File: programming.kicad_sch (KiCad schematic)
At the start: 14 parts, among them U1 LFE5U-12F-6BG256C, U2 AT25SF081-SSHD-X

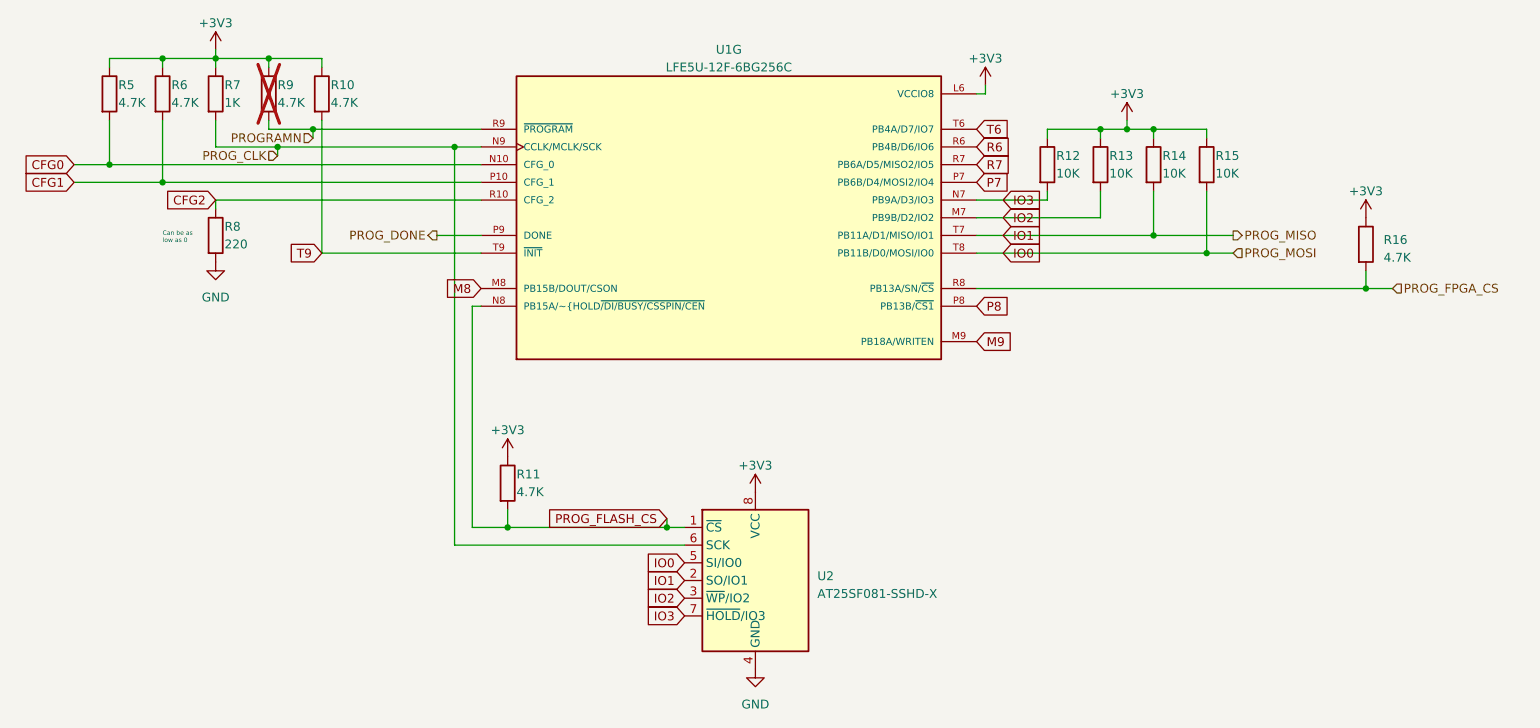
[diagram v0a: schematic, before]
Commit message: Small routing tweaks, add breakout to schematic
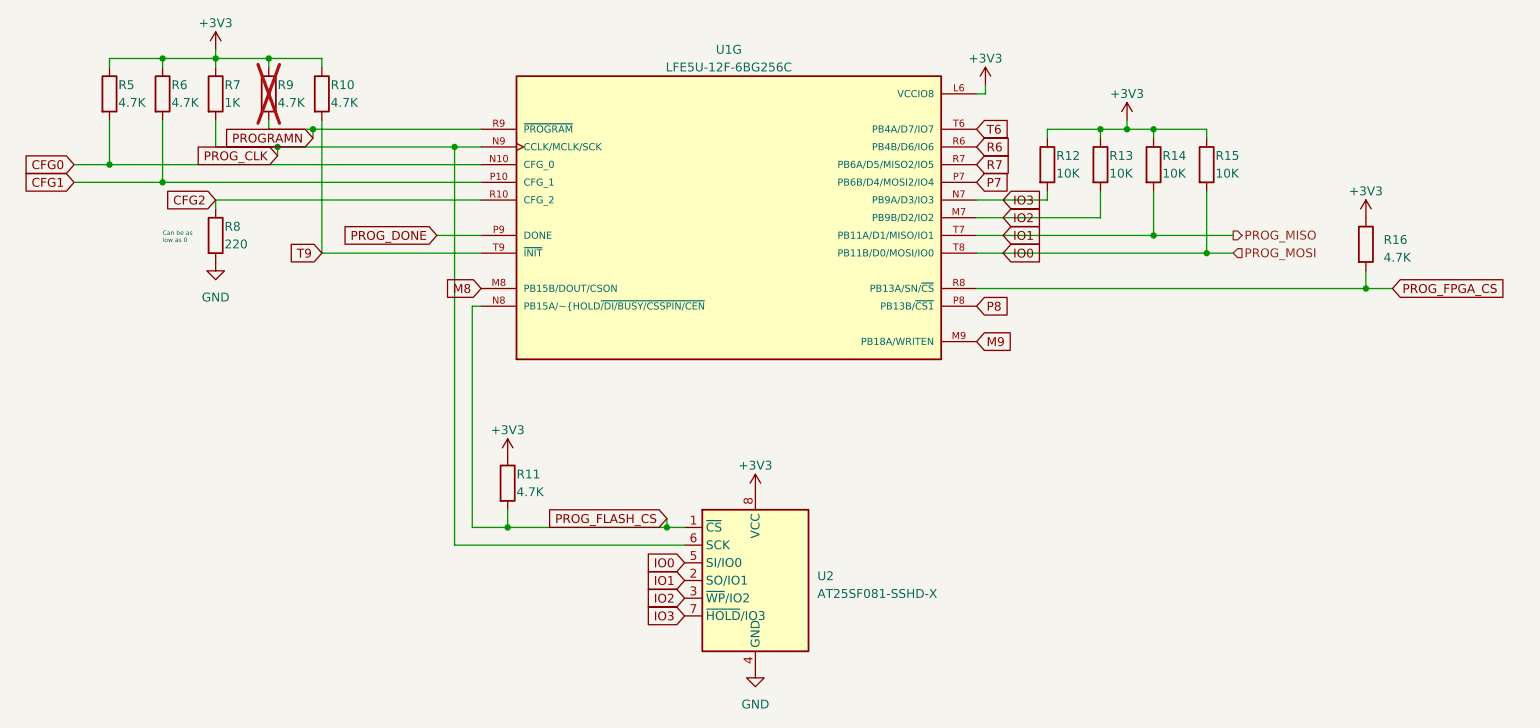
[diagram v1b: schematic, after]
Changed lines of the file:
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@@
     (effects (font (size 0.635 0.635)) (justify left bottom))
+  )
+  (global_label "PROG_FPGA_CS" (shape input) (at 242.57 85.09 0) (fields_autoplaced)
+    (effects (font (size 1.27 1.27)) (justify left))
+    (property "Intersheetrefs" "${INTERSHEET_REFS}" (at 259.7482 85.09 0)
+      (effects (font (size 1.27 1.27)) (justify left) hide)
+    )
   )
   (global_label "IO2" (shape input) (at 140.97 129.54 180) (fields_autoplaced)
@@
     )
   )
+  (global_label "PROG_DONE" (shape input) (at 105.41 77.47 180) (fields_autoplaced)
+    (effects (font (size 1.27 1.27)) (justify right))
+    (property "Intersheetrefs" "${INTERSHEET_REFS}" (at 91.3161 77.47 0)
+      (effects (font (size 1.27 1.27)) (justify right) hide)
+    )
+  )
   (global_label "M8" (shape input) (at 111.76 85.09 180) (fields_autoplaced)
     (effects (font (size 1.27 1.27)) (justify right))
@@
     )
   )
-  (hierarchical_label "PROG_DONE" (shape output) (at 105.41 77.47 180) (fields_autoplaced)
+  (global_label "PROGRAMN" (shape input) (at 87.63 63.5 180) (fields_autoplaced)
     (effects (font (size 1.27 1.27)) (justify right))
+    (property "Intersheetrefs" "${INTERSHEET_REFS}" (at 74.4432 63.5 0)
+      (effects (font (size 1.27 1.27)) (justify right) hide)
+    )
   )
-  (hierarchical_label "PROGRAMN" (shape input) (at 87.63 63.5 180) (fields_autoplaced)
+  (global_label "PROG_CLK" (shape input) (at 82.55 66.04 180) (fields_autoplaced)
     (effects (font (size 1.27 1.27)) (justify right))
+    (property "Intersheetrefs" "${INTERSHEET_REFS}" (at 69.968 66.04 0)
+      (effects (font (size 1.27 1.27)) (justify right) hide)
+    )
+  )
+  (hierarchical_label "PROG_MOSI" (shape input) (at 219.71 80.01 0) (fields_autoplaced)
+    (effects (font (size 1.27 1.27)) (justify left))
   )
   (hierarchical_label "PROG_MISO" (shape output) (at 219.71 77.47 0) (fields_autoplaced)
     (effects (font (size 1.27 1.27)) (justify left))
   )
-  (hierarchical_label "PROG_MOSI" (shape input) (at 219.71 80.01 0) (fields_autoplaced)
-    (effects (font (size 1.27 1.27)) (justify left))
-  )
-  (hierarchical_label "PROG_FPGA_CS" (shape input) (at 242.57 85.09 0) (fields_autoplaced)
-    (effects (font (size 1.27 1.27)) (justify left))
-  )
-  (hierarchical_label "PROG_CLK" (shape input) (at 82.55 66.04 180) (fields_autoplaced)
-    (effects (font (size 1.27 1.27)) (justify right))
-  )
   (symbol (lib_id "Device:R") (at 88.9 57.15 0) (unit 1)

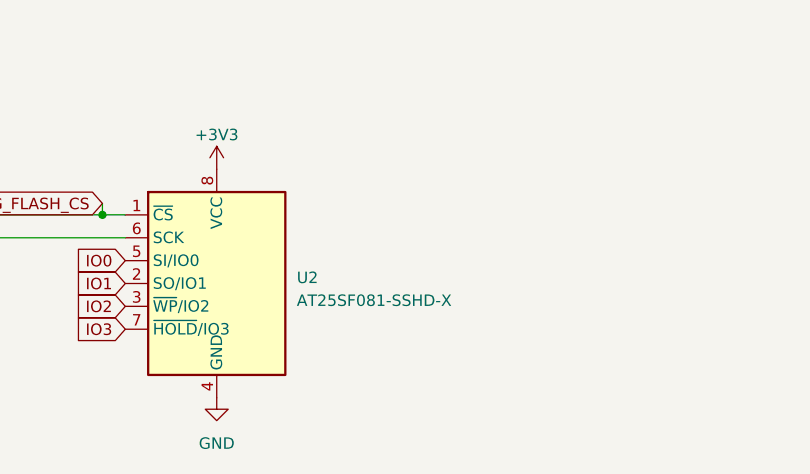
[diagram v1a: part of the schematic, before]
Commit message: Route flash + jtag resistors
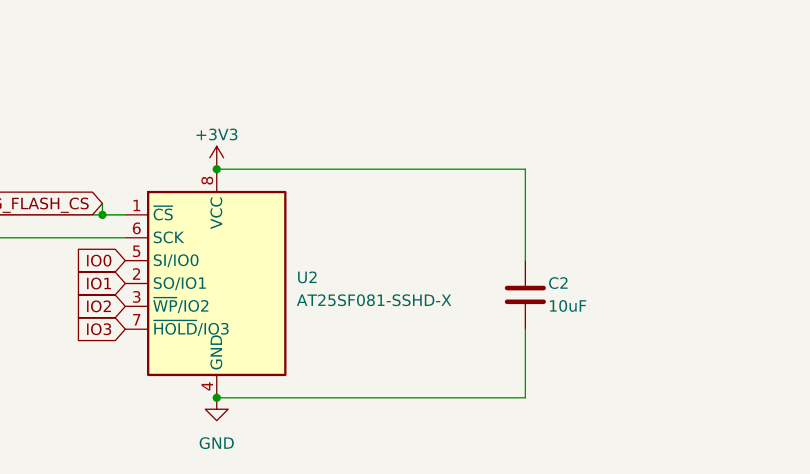
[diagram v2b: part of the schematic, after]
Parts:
- added C2: 10uF, Capacitor_SMD:C_0603_1608Metric, symbol Device:C
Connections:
- net +3V3: now also C2.1
- net GND: now also C2.2
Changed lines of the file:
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@@
   (junction (at 81.28 52.07) (diameter 0) (color 0 0 0 0)
   )
+  (junction (at 151.13 114.3) (diameter 0) (color 0 0 0 0)
+  )
   (junction (at 66.04 52.07) (diameter 0) (color 0 0 0 0)
   )
@@
   (junction (at 107.95 64.77) (diameter 0) (color 0 0 0 0)
   )
+  (junction (at 151.13 139.7) (diameter 0) (color 0 0 0 0)
+  )
   (junction (at 208.28 62.23) (diameter 0) (color 0 0 0 0)
   )
@@
   (junction (at 138.43 119.38) (diameter 0) (color 0 0 0 0)
   )
+  (wire (pts (xy 185.42 124.46) (xy 185.42 114.3))
+    (stroke (width 0) (type default))
+  )
   (wire (pts (xy 115.57 116.84) (xy 115.57 119.38))
     (stroke (width 0) (type default))
@@
     (stroke (width 0) (type default))
   )
+  (wire (pts (xy 185.42 114.3) (xy 151.13 114.3))
+    (stroke (width 0) (type default))
+  )
   (wire (pts (xy 208.28 62.23) (xy 215.9 62.23))
     (stroke (width 0) (type default))
@@
     (stroke (width 0) (type default))
   )
+  (wire (pts (xy 185.42 139.7) (xy 151.13 139.7))
+    (stroke (width 0) (type default))
+  )
   (wire (pts (xy 66.04 60.96) (xy 66.04 69.85))
+    (stroke (width 0) (type default))
+  )
+  (wire (pts (xy 185.42 132.08) (xy 185.42 139.7))
     (stroke (width 0) (type default))
   )
@@
         )
       )
+    )
+  )
+  (symbol (lib_id "Device:C") (at 185.42 128.27 0) (unit 1)
+    (in_bom yes) (on_board yes) (dnp no)
+    (property "Reference" "C2" (at 187.96 127 0)
+      (effects (font (size 1.27 1.27)) (justify left))
+    )
+    (property "Value" "10uF" (at 187.96 129.54 0)
+      (effects (font (size 1.27 1.27)) (justify left))
+    )
+    (property "Footprint" "Capacitor_SMD:C_0603_1608Metric" (at 186.3852 132.08 0)
+      (effects (font (size 1.27 1.27)) hide)
+    )
+    (property "Datasheet" "~" (at 185.42 128.27 0)
+      (effects (font (size 1.27 1.27)) hide)
+    )
+    (pin "1")
+    (pin "2")
+    (instances
+      (project "daughterboard"
+        (path "/dce8b7ce-114c-4680-a1bd-14f36a94838a/233da297-15ca-4163-a51b-09f27dce3135"
+          (reference "C2") (unit 1)
+        )
+        (path "/dce8b7ce-114c-4680-a1bd-14f36a94838a/60bc7ad5-be18-49b3-905c-1be058d9dfc0"
+          (reference "C9") (unit 1)
+        )
+      )

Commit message: Route power
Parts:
- C2: footprint Capacitor_SMD:C_0603_1608Metric -> Capacitor_SMD:C_0805_2012Metric
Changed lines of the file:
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@@
       (effects (font (size 1.27 1.27)) (justify left))
     )
-    (property "Footprint" "Capacitor_SMD:C_0603_1608Metric" (at 186.3852 132.08 0)
+    (property "Footprint" "Capacitor_SMD:C_0805_2012Metric" (at 186.3852 132.08 0)
       (effects (font (size 1.27 1.27)) hide)
     )

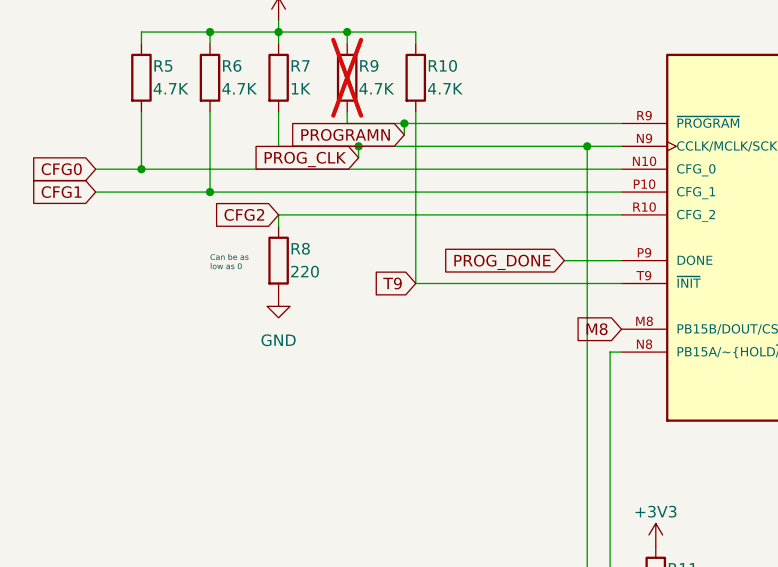
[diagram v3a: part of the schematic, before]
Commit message: Move programming pins to 100 mil headers
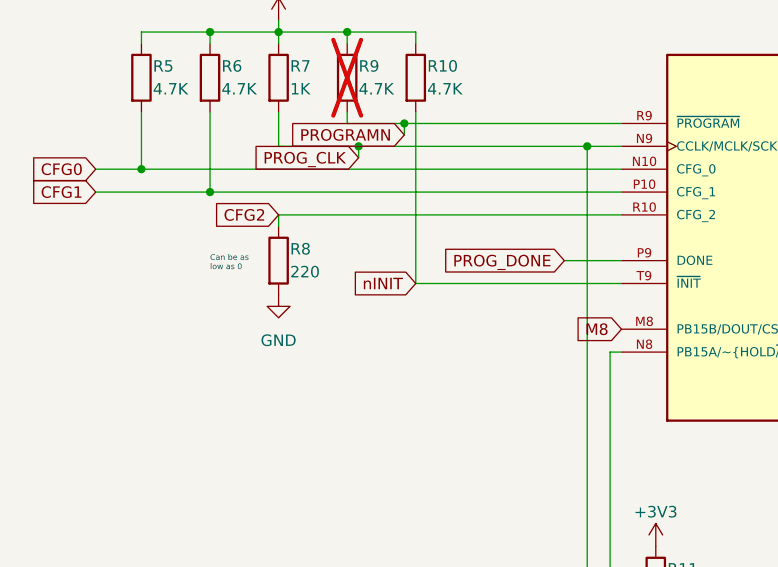
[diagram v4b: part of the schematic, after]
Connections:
- net T9 renamed nINIT
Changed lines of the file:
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@@
     )
   )
-  (global_label "T9" (shape input) (at 88.9 80.01 180) (fields_autoplaced)
+  (global_label "nINIT" (shape input) (at 88.9 80.01 180) (fields_autoplaced)
     (effects (font (size 1.27 1.27)) (justify right))
-    (property "Intersheetrefs" "${INTERSHEET_REFS}" (at 83.8171 80.01 0)
+    (property "Intersheetrefs" "${INTERSHEET_REFS}" (at 81.3375 80.01 0)
       (effects (font (size 1.27 1.27)) (justify right) hide)
     )

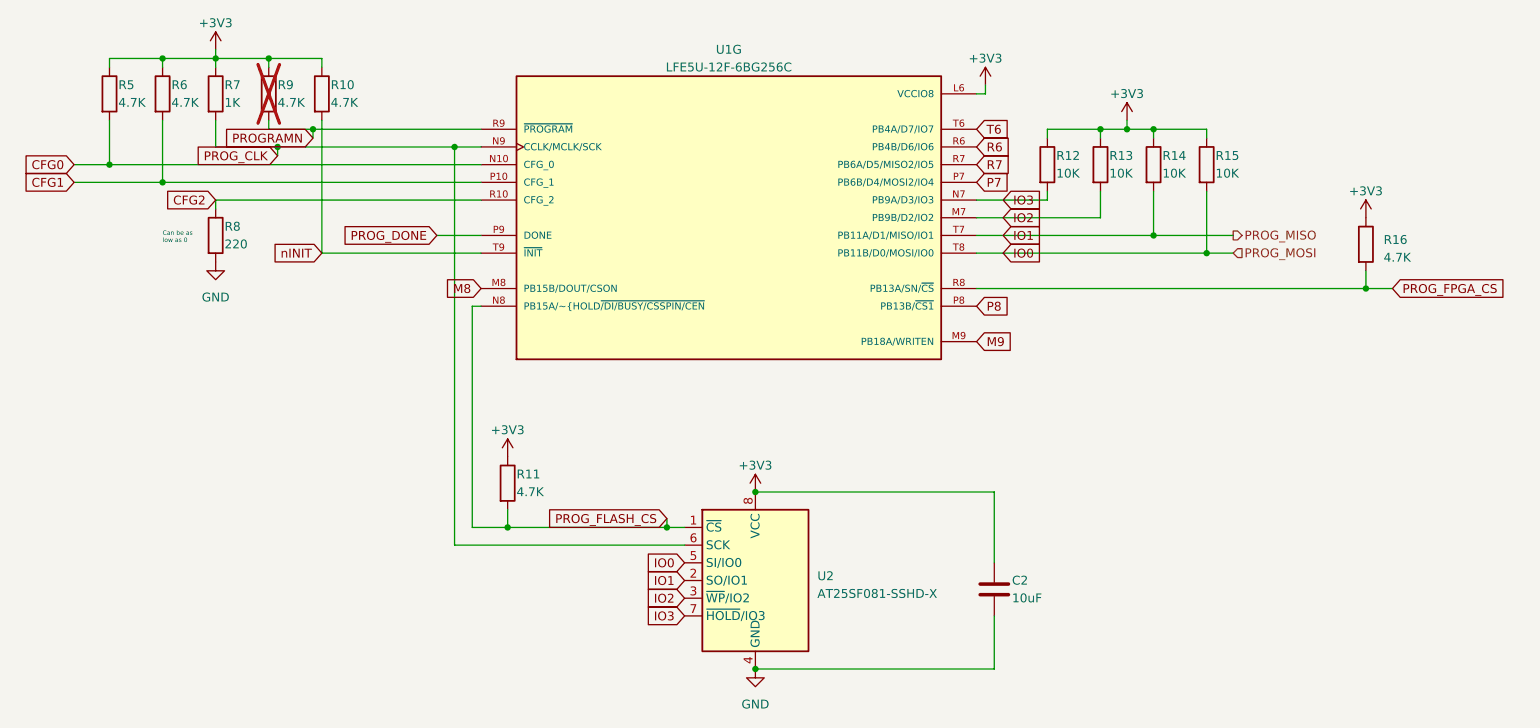
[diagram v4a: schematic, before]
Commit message: Route power, FTDI chip
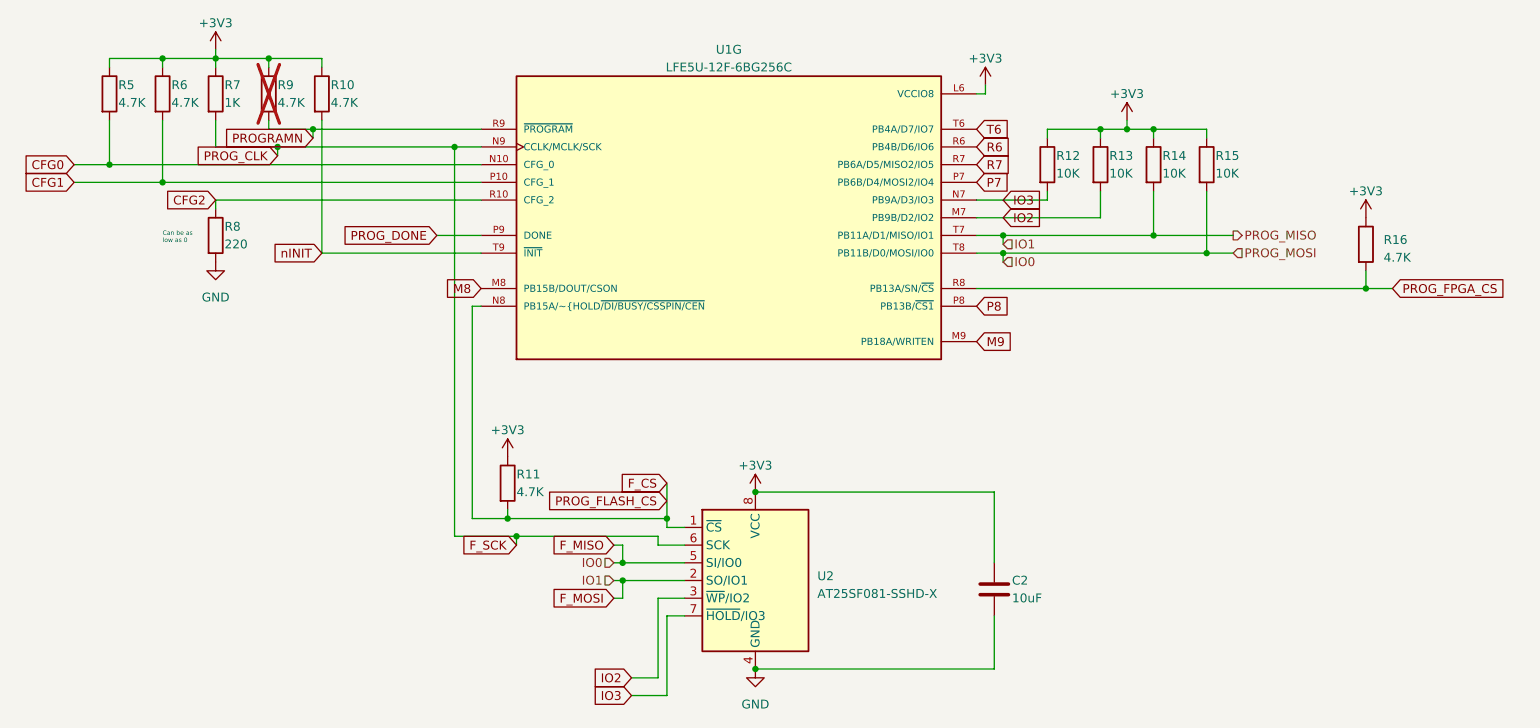
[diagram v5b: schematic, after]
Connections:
- net IO0 renamed F_MISO
- net IO1 renamed F_MOSI
- net PROG_CLK renamed F_SCK
- net PROG_FLASH_CS renamed F_CS
